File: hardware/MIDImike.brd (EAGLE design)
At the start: 84.8 x 53.3 mm, 5 parts, among them SW1 PUSH-BTN

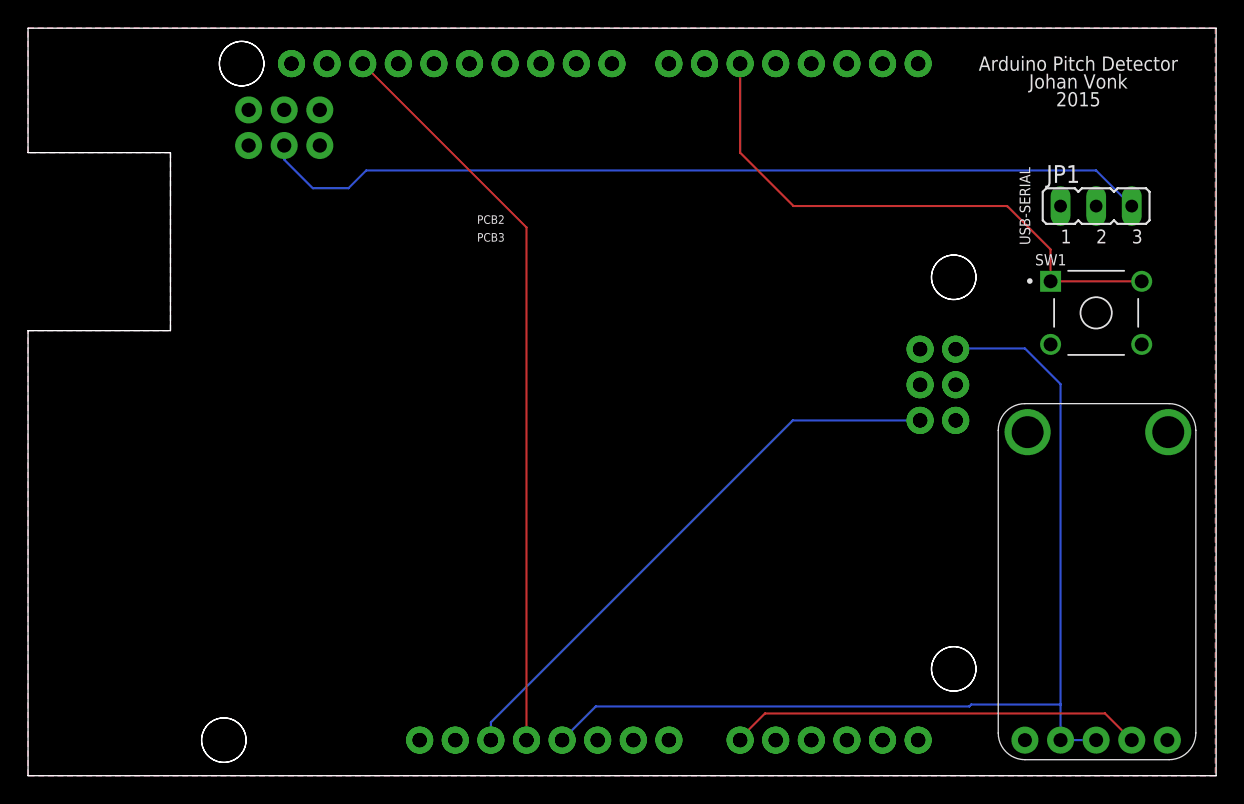
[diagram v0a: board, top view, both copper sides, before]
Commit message: fix low notes; clean up
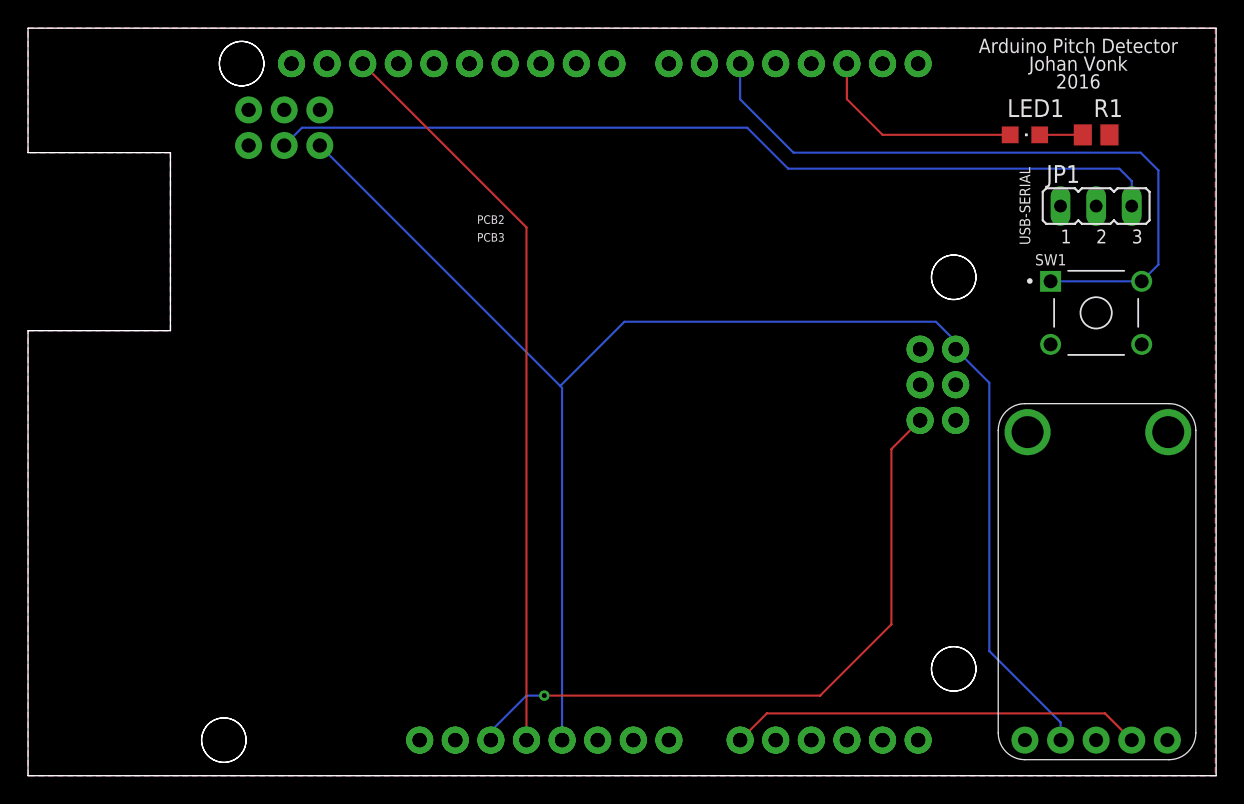
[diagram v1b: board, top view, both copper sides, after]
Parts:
- added LED1: AMBER, OPNpool:CHIPLED_0805
- added R1: 330Ω, rcl:R0805
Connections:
- new net N$1: LED1.A, PCB2.D2
- new net N$8: LED1.C, R1.2
- net 5V: no longer PCB1.3
- net GND: now also PCB1.3, R1.1
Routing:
- net 5V: track 73.1 -> 111.8 mm
- net N$1: track 0.00 -> 15.2 mm
- net REPLAY: track 40.1 -> 49.4 mm
- net N$7: track 40.8 -> 47.9 mm, vias 0 -> 1
- net N$8: track 0.00 -> 3.08 mm
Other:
- board text added: "2016"
- board text removed: "2015"
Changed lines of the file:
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@@
 <setting verticaltext="up"/>
 </settings>
-<grid distance="50" unitdist="mil" unit="mil" style="lines" multiple="1" display="no" altdistance="5" altunitdist="mil" altunit="mil"/>
+<grid distance="25" unitdist="mil" unit="mil" style="lines" multiple="1" display="no" altdistance="5" altunitdist="mil" altunit="mil"/>
 <layers>
 <layer number="1" name="Top" color="4" fill="1" visible="yes" active="yes"/>
@@
 <text x="81.28" y="40.64" size="0.762" layer="22" rot="R90" align="center">USB-MIDI</text>
 <text x="71.12" y="40.64" size="0.762" layer="21" rot="R90" align="center">USB-SERIAL</text>
-<text x="74.93" y="50.8" size="1.016" layer="21" align="center">Arduino Pitch Detector</text>
-<text x="74.93" y="49.53" size="1.016" layer="21" align="center">Johan Vonk</text>
-<text x="74.93" y="48.26" size="1.016" layer="21" align="center">2015</text>
+<text x="74.93" y="52.07" size="1.016" layer="21" align="center">Arduino Pitch Detector</text>
+<text x="74.93" y="50.8" size="1.016" layer="21" align="center">Johan Vonk</text>
+<text x="74.93" y="49.53" size="1.016" layer="21" align="center">2016</text>
 <text x="53.34" y="25.4" size="1.27" layer="22" rot="MR0">https://github.com/jvonk/Arduino_Pitch-Detector</text>
 </plain>
@@
 <attribute name="VALUE" x="72.644" y="36.322" size="1.27" layer="27" ratio="10"/>
 </element>
+<element name="R1" library="rcl" library_urn="urn:adsk.eagle:library:334" package="R0805" package3d_urn="urn:adsk.eagle:package:23553/2" value="330Ω" x="76.2" y="45.72" smashed="yes" rot="R180">
+<attribute name="MANF" value="Bourns" x="76.2" y="45.72" size="1.778" layer="27" rot="R180" display="off"/>
+<attribute name="MANF#" value="CRM0805-JW-1R5ELF" x="76.2" y="45.72" size="1.778" layer="27" rot="R180" display="off"/>
+<attribute name="MOUSER#" value="652-CRM0805JW1R5ELF" x="76.2" y="45.72" size="1.778" layer="27" rot="R180" display="off"/>
+<attribute name="NAME" x="78.105" y="48.26" size="1.27" layer="25" rot="R180"/>
+<attribute name="POPULARITY" value="86" x="76.2" y="45.72" size="1.778" layer="27" rot="R180" display="off"/>
+<attribute name="SPICEPREFIX" value="R" x="76.2" y="45.72" size="1.778" layer="27" rot="R180" display="off"/>
+<attribute name="VALUE" x="76.835" y="48.26" size="1.27" layer="27" rot="R180"/>
+</element>
+<element name="LED1" library="OPNpool" package="CHIPLED_0805" package3d_urn="urn:adsk.eagle:package:15821/2" value="AMBER" x="71.12" y="45.72" smashed="yes" rot="R270">
+<attribute name="NAME" x="69.85" y="46.99" size="1.27" layer="25"/>
+<attribute name="POPULARITY" value="52" x="71.12" y="45.72" size="1.778" layer="27" rot="R270" display="off"/>
+<attribute name="VALUE" x="69.85" y="43.18" size="1.27" layer="27"/>
+</element>
 </elements>
 <signals>
@@
 <vertex x="10.16" y="44.45"/>
 </polygon>
+<contactref element="R1" pad="1"/>
+<contactref element="PCB1" pad="3"/>
 </signal>
 <signal name="5V">
@@
 <contactref element="PCB3" pad="5V"/>
 <contactref element="PCB3" pad="5V@1"/>
-<wire x1="73.66" y1="27.94" x2="71.12" y2="30.48" width="0.1524" layer="16"/>
-<wire x1="71.12" y1="30.48" x2="66.23001875" y2="30.48" width="0.1524" layer="16"/>
-<wire x1="66.23001875" y1="30.48" x2="66.18000625" y2="30.4299875" width="0.1524" layer="16"/>
-<wire x1="73.66" y1="2.54" x2="73.66" y2="5.08" width="0.1524" layer="16"/>
-<contactref element="PCB1" pad="3"/>
-<wire x1="73.66" y1="5.08" x2="73.66" y2="27.94" width="0.1524" layer="16"/>
-<wire x1="76.2" y1="2.54" x2="73.66" y2="2.54" width="0.1524" layer="16"/>
-<wire x1="67.14996875" y1="4.9403" x2="67.28966875" y2="5.08" width="0.1524" layer="16"/>
-<wire x1="67.28966875" y1="5.08" x2="73.66" y2="5.08" width="0.1524" layer="16"/>
-<wire x1="38.1" y1="2.54" x2="40.5003" y2="4.9403" width="0.1524" layer="16"/>
-<wire x1="40.5003" y1="4.9403" x2="67.14996875" y2="4.9403" width="0.1524" layer="16"/>
+<wire x1="66.18000625" y1="30.4299875" x2="68.58" y2="28.02999375" width="0.1524" layer="16"/>
+<wire x1="68.58" y1="28.02999375" x2="68.58" y2="8.89" width="0.1524" layer="16"/>
+<wire x1="68.58" y1="8.89" x2="73.66" y2="3.81" width="0.1524" layer="16"/>
+<wire x1="73.66" y1="3.81" x2="73.66" y2="2.54" width="0.1524" layer="16"/>
+<wire x1="20.81560625" y1="44.9587875" x2="37.967196875" y2="27.807196875" width="0.1524" layer="16"/>
+<wire x1="37.967196875" y1="27.807196875" x2="38.1" y2="27.67439375" width="0.1524" layer="16"/>
+<wire x1="38.1" y1="27.67439375" x2="38.1" y2="2.54" width="0.1524" layer="16"/>
+<wire x1="37.967196875" y1="27.807196875" x2="42.545" y2="32.385" width="0.1524" layer="16"/>
+<wire x1="42.545" y1="32.385" x2="64.77" y2="32.385" width="0.1524" layer="16"/>
+<wire x1="64.77" y1="32.385" x2="66.18000625" y2="30.97499375" width="0.1524" layer="16"/>
+<wire x1="66.18000625" y1="30.97499375" x2="66.18000625" y2="30.4299875" width="0.1524" layer="16"/>
 </signal>
 <signal name="A0">
 <contactref element="PCB1" pad="4"/>
 <contactref element="PCB2" pad="A0"/>
-<wire x1="50.8" y1="2.54" x2="50.8" y2="2.667" width="0.1524" layer="1"/>
-<wire x1="50.8" y1="2.667" x2="52.578" y2="4.445" width="0.1524" layer="1"/>
-<wire x1="52.578" y1="4.445" x2="76.835" y2="4.445" width="0.1524" layer="1"/>
-<wire x1="76.835" y1="4.445" x2="78.74" y2="2.54" width="0.1524" layer="1"/>
+<wire x1="78.74" y1="2.54" x2="76.835" y2="4.445" width="0.1524" layer="1"/>
+<wire x1="50.8" y1="2.54" x2="52.705" y2="4.445" width="0.1524" layer="1"/>
+<wire x1="52.705" y1="4.445" x2="76.835" y2="4.445" width="0.1524" layer="1"/>
 </signal>
 <signal name="3.3V">
@@
 <contactref element="PCB2" pad="!RESET!"/>
 <contactref element="PCB2" pad="!RESET!@1"/>
-<wire x1="33.02" y1="2.54" x2="33.02" y2="3.81" width="0.1524" layer="16"/>
-<wire x1="54.5599875" y1="25.3499875" x2="63.64000625" y2="25.3499875" width="0.1524" layer="16"/>
-<wire x1="33.02" y1="3.81" x2="54.5599875" y2="25.3499875" width="0.1524" layer="16"/>
+<wire x1="63.64000625" y1="25.3499875" x2="61.595" y2="23.30498125" width="0.1524" layer="1"/>
+<wire x1="61.595" y1="23.30498125" x2="61.595" y2="10.795" width="0.1524" layer="1"/>
+<wire x1="61.595" y1="10.795" x2="56.515" y2="5.715" width="0.1524" layer="1"/>
+<wire x1="56.515" y1="5.715" x2="36.83" y2="5.715" width="0.1524" layer="1"/>
+<via x="36.83" y="5.715" extent="1-16" drill="0.35"/>
+<wire x1="35.56" y1="5.715" x2="33.0581" y2="3.2131" width="0.1524" layer="16"/>
+<wire x1="33.0581" y1="3.2131" x2="33.02" y2="3.175" width="0.1524" layer="16"/>
+<wire x1="36.83" y1="5.715" x2="35.56" y2="5.715" width="0.1524" layer="16"/>
+<wire x1="33.0708" y1="2.5908" x2="33.02" y2="2.54" width="0.1524" layer="1"/>
+<wire x1="33.0708" y1="3.2004" x2="33.0708" y2="2.5908" width="0.1524" layer="16"/>
+<wire x1="33.0708" y1="2.5908" x2="33.02" y2="2.54" width="0.1524" layer="16"/>
+<wire x1="33.0708" y1="3.2004" x2="33.0581" y2="3.2131" width="0.1524" layer="16"/>
 </signal>
 <signal name="N$4">
@@
 <contactref element="SW1" pad="1@1"/>
 <contactref element="PCB2" pad="D5"/>
-<wire x1="72.95" y1="35.27" x2="79.45" y2="35.27" width="0.1524" layer="1"/>
-<wire x1="72.95" y1="35.27" x2="72.95" y2="37.54" width="0.1524" layer="1"/>
-<wire x1="72.95" y1="37.54" x2="69.85" y2="40.64" width="0.1524" layer="1"/>
-<wire x1="50.8" y1="44.45" x2="54.61" y2="40.64" width="0.1524" layer="1"/>
-<wire x1="69.85" y1="40.64" x2="54.61" y2="40.64" width="0.1524" layer="1"/>
-<wire x1="50.8" y1="50.8" x2="50.8" y2="44.45" width="0.1524" layer="1"/>
+<wire x1="50.8" y1="50.8" x2="50.8" y2="48.26" width="0.1524" layer="16"/>
+<wire x1="50.8" y1="48.26" x2="54.61" y2="44.45" width="0.1524" layer="16"/>
+<wire x1="54.61" y1="44.45" x2="79.375" y2="44.45" width="0.1524" layer="16"/>
+<wire x1="79.375" y1="44.45" x2="80.645" y2="43.18" width="0.1524" layer="16"/>
+<wire x1="80.645" y1="36.465" x2="79.45" y2="35.27" width="0.1524" layer="16"/>
+<wire x1="80.645" y1="43.18" x2="80.645" y2="36.465" width="0.1524" layer="16"/>
+<wire x1="79.45" y1="35.27" x2="72.95" y2="35.27" width="0.1524" layer="16"/>
 </signal>
 <signal name="N$3">
 <contactref element="PCB2" pad="MOSI2"/>
 <contactref element="JP1" pad="3"/>
-<wire x1="78.74" y1="40.64" x2="76.2" y2="43.18" width="0.1524" layer="16"/>
-<wire x1="76.2" y1="43.18" x2="24.13" y2="43.18" width="0.1524" layer="16"/>
-<wire x1="24.13" y1="43.18" x2="22.86" y2="41.91" width="0.1524" layer="16"/>
-<wire x1="22.86" y1="41.91" x2="20.32" y2="41.91" width="0.1524" layer="16"/>
-<wire x1="20.32" y1="41.91" x2="18.27560625" y2="43.95439375" width="0.1524" layer="16"/>
-<wire x1="18.27560625" y1="43.95439375" x2="18.27560625" y2="44.9587875" width="0.1524" layer="16"/>
+<wire x1="18.27560625" y1="44.9587875" x2="19.54481875" y2="46.228" width="0.1524" layer="16"/>
+<wire x1="51.308" y1="46.228" x2="54.229" y2="43.307" width="0.1524" layer="16"/>
+<wire x1="77.851" y1="43.307" x2="78.74" y2="42.418" width="0.1524" layer="16"/>
+<wire x1="78.74" y1="42.418" x2="78.74" y2="40.64" width="0.1524" layer="16"/>
+<wire x1="19.54481875" y1="46.228" x2="51.308" y2="46.228" width="0.1524" layer="16"/>
+<wire x1="54.229" y1="43.307" x2="77.851" y2="43.307" width="0.1524" layer="16"/>
+</signal>
+<signal name="N$1">
+<contactref element="PCB2" pad="D2"/>
+<contactref element="LED1" pad="A"/>
+<wire x1="58.42" y1="50.8" x2="58.42" y2="48.26" width="0.1524" layer="1"/>
+<wire x1="58.42" y1="48.26" x2="60.96" y2="45.72" width="0.1524" layer="1"/>
+<wire x1="60.96" y1="45.72" x2="70.07" y2="45.72" width="0.1524" layer="1"/>
+</signal>
+<signal name="N$8">
+<contactref element="LED1" pad="C"/>
+<contactref element="R1" pad="2"/>
+<wire x1="72.17" y1="45.72" x2="75.25" y2="45.72" width="0.1524" layer="1"/>
 </signal>
 </signals>
@@
 </drawing>
 <compatibility>
+<note version="8.2" severity="warning">
+Since Version 8.2, EAGLE supports online libraries. The ids
+of those online libraries will not be understood (or retained)
+with this version.
+</note>
 <note version="8.3" severity="warning">
 Since Version 8.3, EAGLE supports URNs for individual library
